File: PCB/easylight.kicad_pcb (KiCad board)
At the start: 2 copper layers, 50.2 x 41.3 mm, 49 parts, among them J1 LiPo (1S/3.7V), J2 USB/PWR, J3 LEDs, J4 AVR-ISP, J5 SW1, J6 SW1, J7 SW1, Q1 AO3415_C181094, Q2 AO3415_C181094, SW0 SPEF110100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

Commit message: add additional capacitor, make data resistors 470R, add template texts in preparation for KiCAD 6, extend readme
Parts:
- added C8: 100uF, Capacitor_SMD:C_1206_3216Metric_Pad1.42x1.75mm_HandSolder, F.Cu at (81.3, 55.9)
- added L1: LOGO, MF custom:mpc_logo_10mm, B.Cu at (52.7, 65.4)
- L1: moved to F.Cu
- R5, R6: value 220 -> 470
- moved L1 26.3 mm to (76.2, 50.8), turned to 0 degrees
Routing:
- net GND: track 14.4 -> 18.8 mm, vias 17 -> 19
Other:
- board text added: "${ISSUE_DATE} ${REVISION}"
- board text added: "MISO SCK RST"
- board text added: "VCC MOSI GND"
- board text added: "{TITLE}"
- board text removed: "EasyLight"
- board text removed: "v2023/01/15"

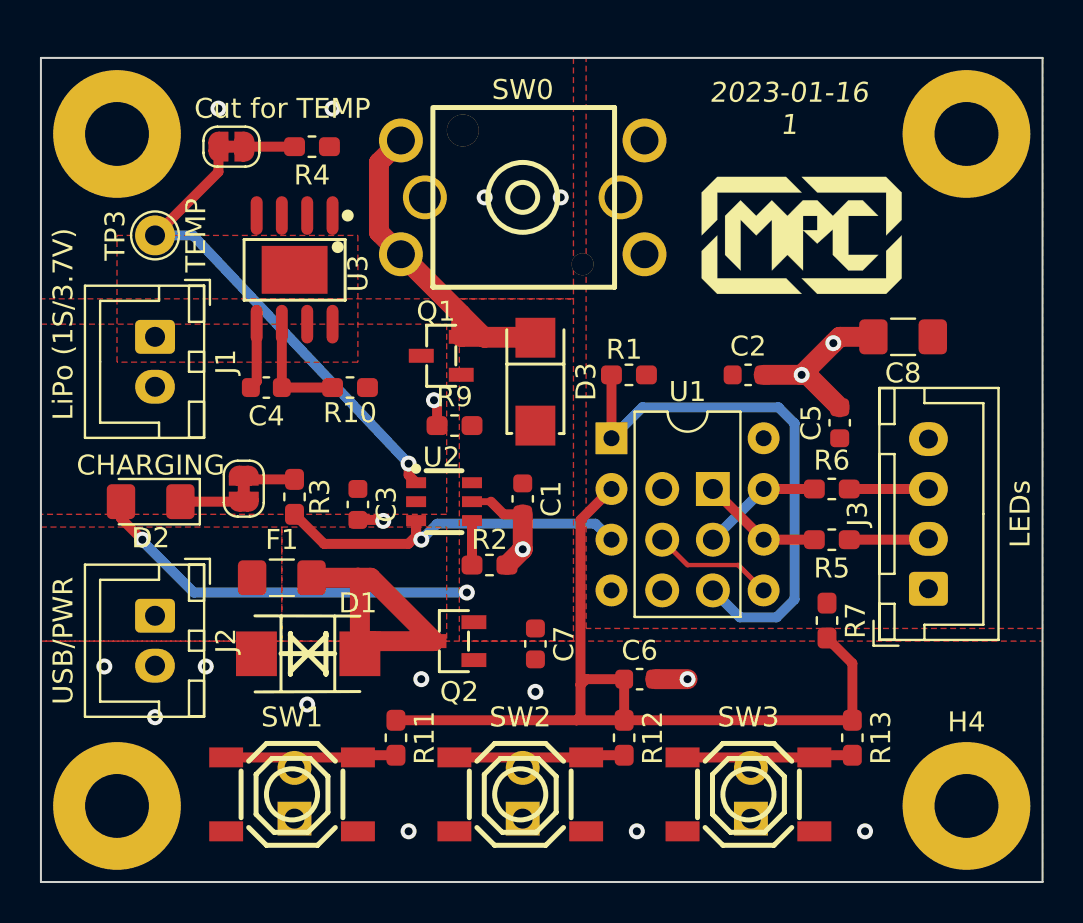
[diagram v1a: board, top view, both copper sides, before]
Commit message: migrate to kicad 6, fix some DRM (clearance still broken), point CI to new files
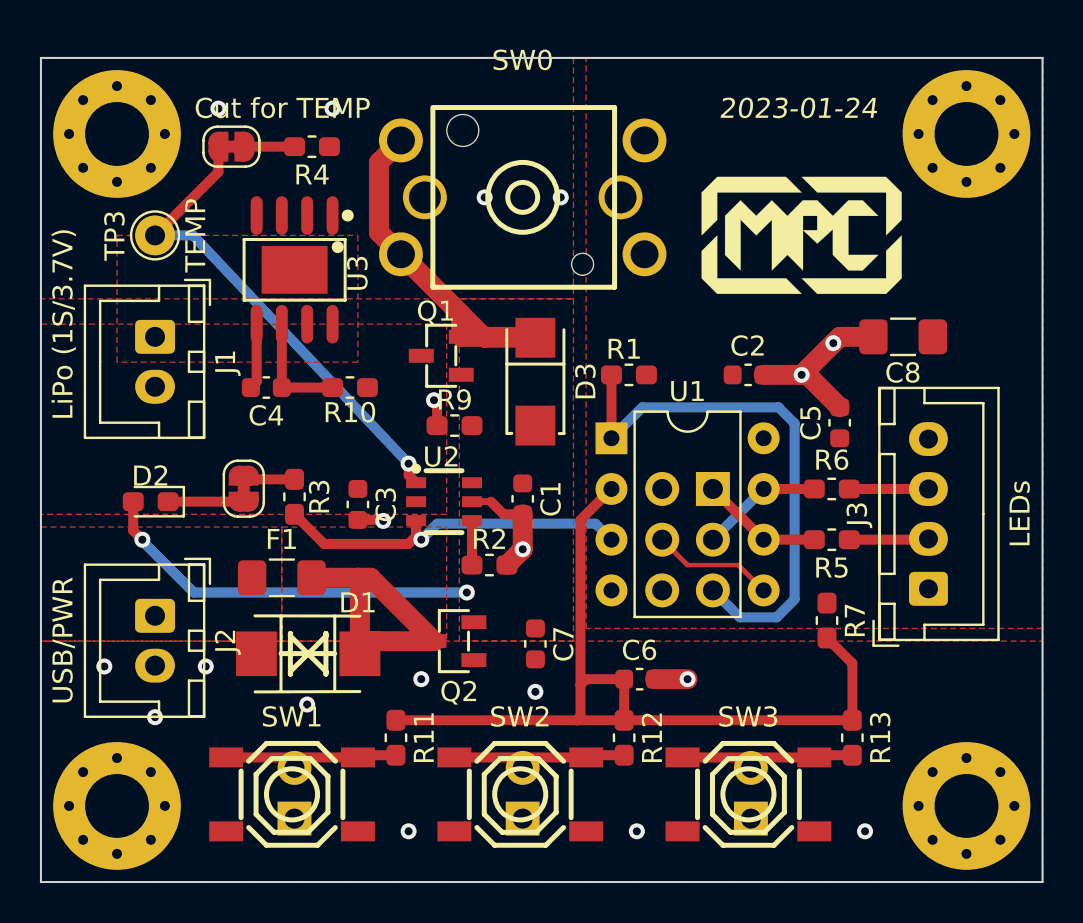
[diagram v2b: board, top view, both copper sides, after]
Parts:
- removed the L1 at (52.7, 65.4)
- added L2: LOGO, ModischFabrications:mpc_logo_10mm, B.Cu at (49.5, 64.8)
- D2: footprint LED_SMD:LED_1206_3216Metric_Pad1.42x1.75mm_HandSolder -> LED_SMD:LED_0603_1608Metric_Pad1.05x0.95mm_HandSolder
- H1, H2, H3, H4: footprint MountingHole:MountingHole_3.2mm_M3_Pad -> ModischFabrications:MountingHole_3.2mm_M3_Pad_Via_NC
- L1: footprint MF custom:mpc_logo_10mm -> ModischFabrications:mpc_logo_10mm
- SW0: footprint lcsc:SW-TH_SPEF110100 -> lcsc:SW-TH_SPEF110100_fixed
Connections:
- SW0 pad 1: (no net) -> unconnected-(SW0-Pad1)
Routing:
- net Net-(JP1-Pad1): track 25.1 -> 24.5 mm
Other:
- net class Default removed
- net class PWR removed
- board text added: "${ISSUE_DATE}"
- board text added: "${TITLE}"
- board text removed: "${ISSUE_DATE} ${REVISION}"
- board text removed: "{TITLE}"

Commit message: relink schematics and footprints, move C, update everything
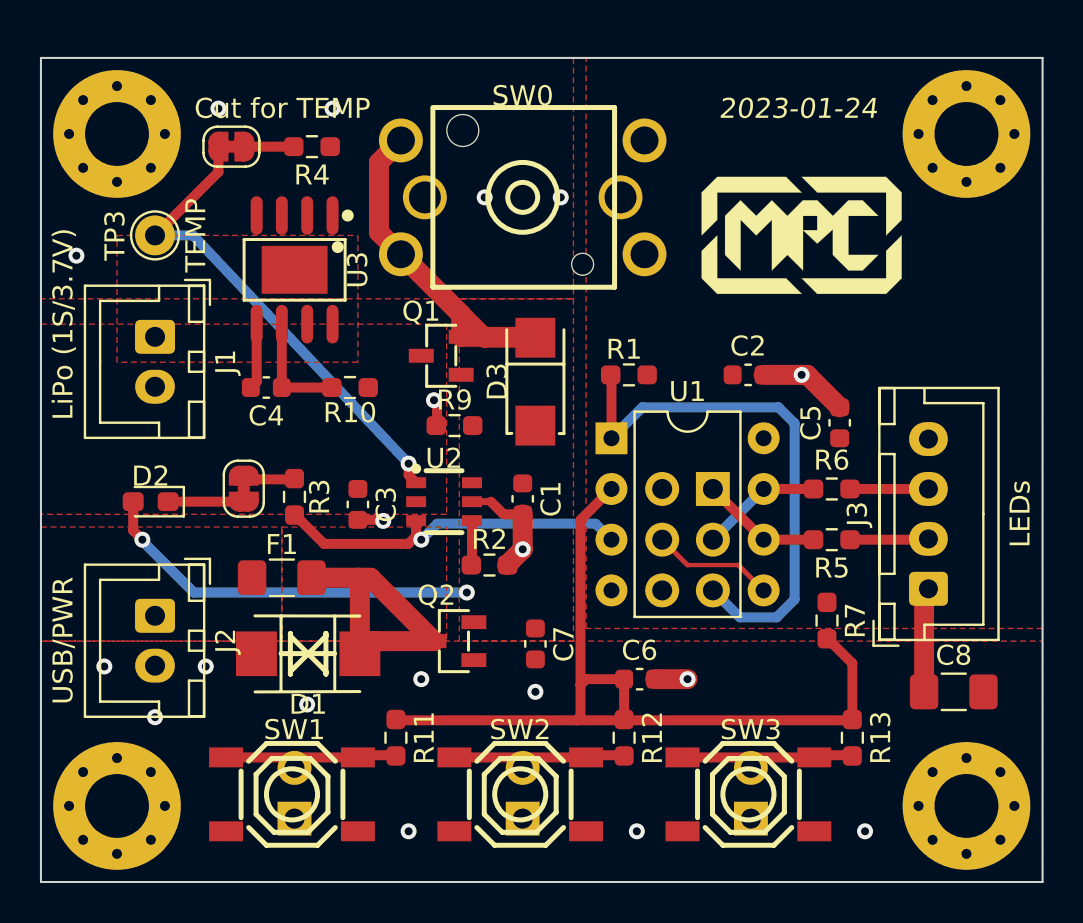
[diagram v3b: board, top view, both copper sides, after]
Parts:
- D1: footprint lcsc:SMB_L4.6-W3.6-LS5.3-BI -> LCSC:SMB_L4.6-W3.6-LS5.3-BI
- D3: footprint lcsc:SMA_L4.3-W2.6-LS5.2-RD -> LCSC:SMA_L4.3-W2.6-LS5.2-RD
- J6: value SW1 -> SW2
- J7: value SW1 -> SW3
- R1, R10, R11, R12, R13, R2, R3, R4, R5, R6, R7, R9: footprint Resistor_SMD:R_0603_1608Metric_Pad1.05x0.95mm_HandSolder -> Resistor_SMD:R_0603_1608Metric_Pad0.98x0.95mm_HandSolder
- SW0: footprint lcsc:SW-TH_SPEF110100_fixed -> LCSC:SW-TH_SPEF110100_fixed
- SW1, SW2, SW3: footprint lcsc:SW-SMD_4P-L5.1-W5.1-P3.70-LS6.5-TL-2 -> LCSC:SW-SMD_4P-L5.1-W5.1-P3.70-LS6.5-TL-2
- U2: footprint lcsc:SOT-23-6_L2.9-W1.6-P0.95-LS2.8-BR -> LCSC:SOT-23-6_L2.9-W1.6-P0.95-LS2.8-BR
- U3: footprint lcsc:SOIC-8_L4.9-W3.9-P1.27-LS6.0-BL-EP3.3-1 -> LCSC:SOIC-8_L4.9-W3.9-P1.27-LS6.0-BL-EP3.3-1
- moved C8 18.0 mm to (83.8, 73.7), turned to 0 degrees
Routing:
- net VCC: track 0.00 -> 5.25 mm
- net GND: track 18.8 -> 14.4 mm

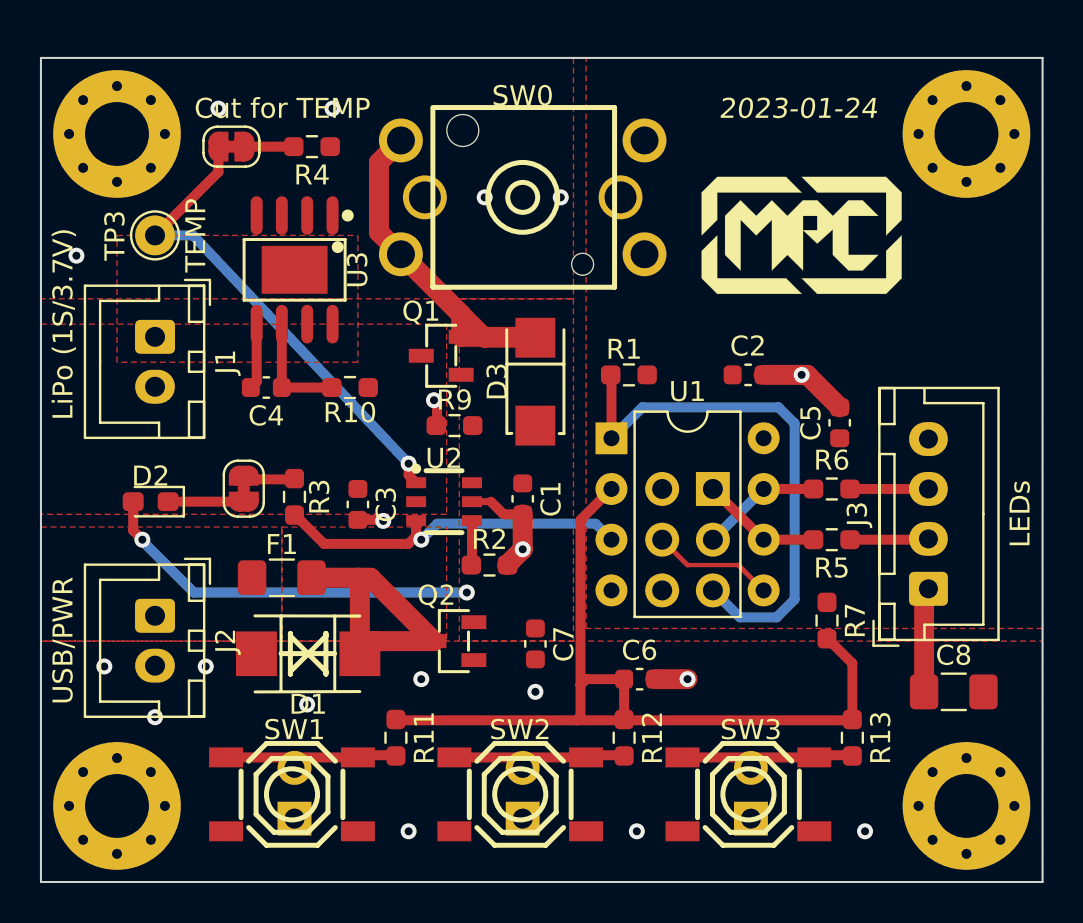
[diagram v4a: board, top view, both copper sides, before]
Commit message: remove colliding connector, add button extension connector, declare v1.0
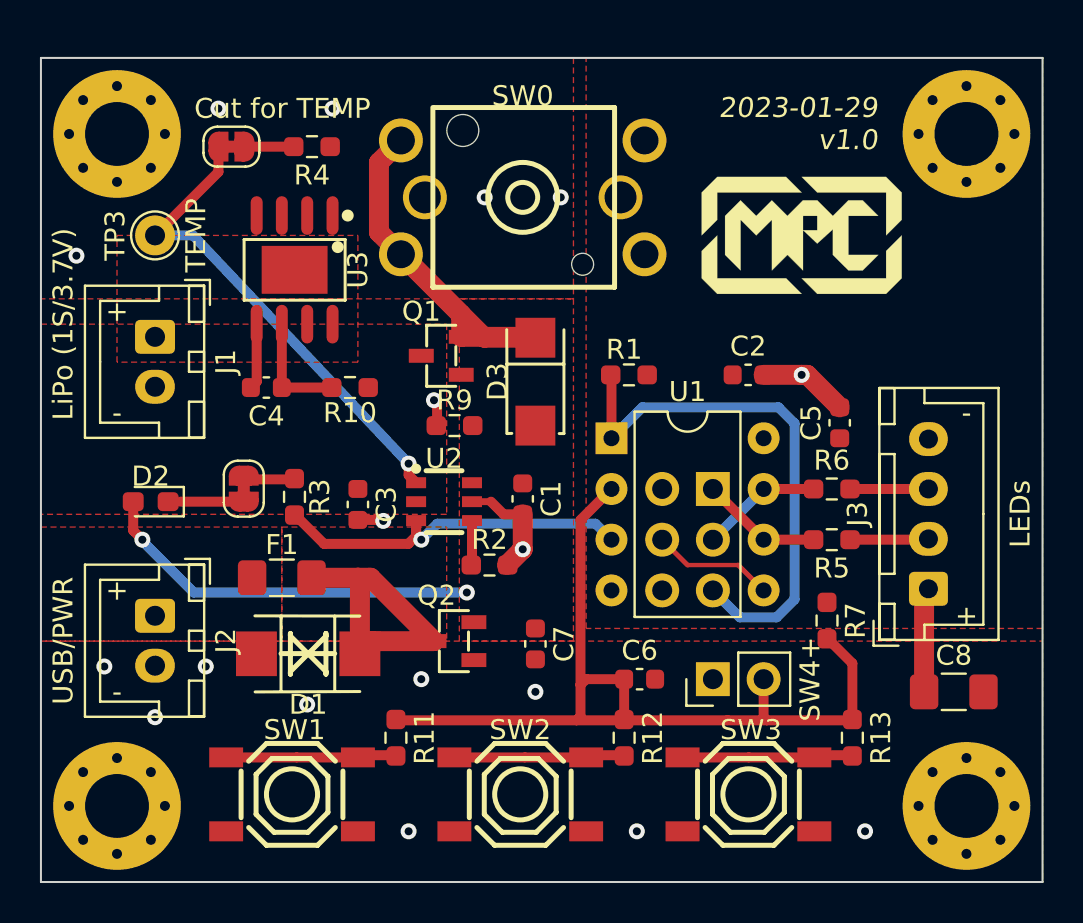
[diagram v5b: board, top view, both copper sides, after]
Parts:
- removed J5: SW1, Connector_PinHeader_2.54mm:PinHeader_1x02_P2.54mm_Vertical
- removed J6: SW2, Connector_PinHeader_2.54mm:PinHeader_1x02_P2.54mm_Vertical
- removed J7: SW3, Connector_PinHeader_2.54mm:PinHeader_1x02_P2.54mm_Vertical
- added J8: SW4+, Connector_PinHeader_2.54mm:PinHeader_1x02_P2.54mm_Vertical, F.Cu at (71.8, 73.0)
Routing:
- net /D_switches: track 44.2 -> 46.3 mm
- net GND: track 14.4 -> 12.8 mm, vias 19 -> 18
- net Net-(R12-Pad2): track 9.12 -> 8.55 mm
- net Net-(R11-Pad2): track 9.12 -> 8.55 mm
- net Net-(R13-Pad2): track 9.12 -> 8.55 mm
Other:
- board text added: "${ISSUE_DATE} v${REVISION}"
- board text removed: "${ISSUE_DATE}"
